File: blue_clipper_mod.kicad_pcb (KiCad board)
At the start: 2 copper layers, 68.6 x 50.8 mm, 23 parts, among them J1 AudioJack3, J2 AudioJack2, SW1 SW_Rotary_1x4_MP, SW2 SW_Rotary_1x4_MP, U1 RC4558

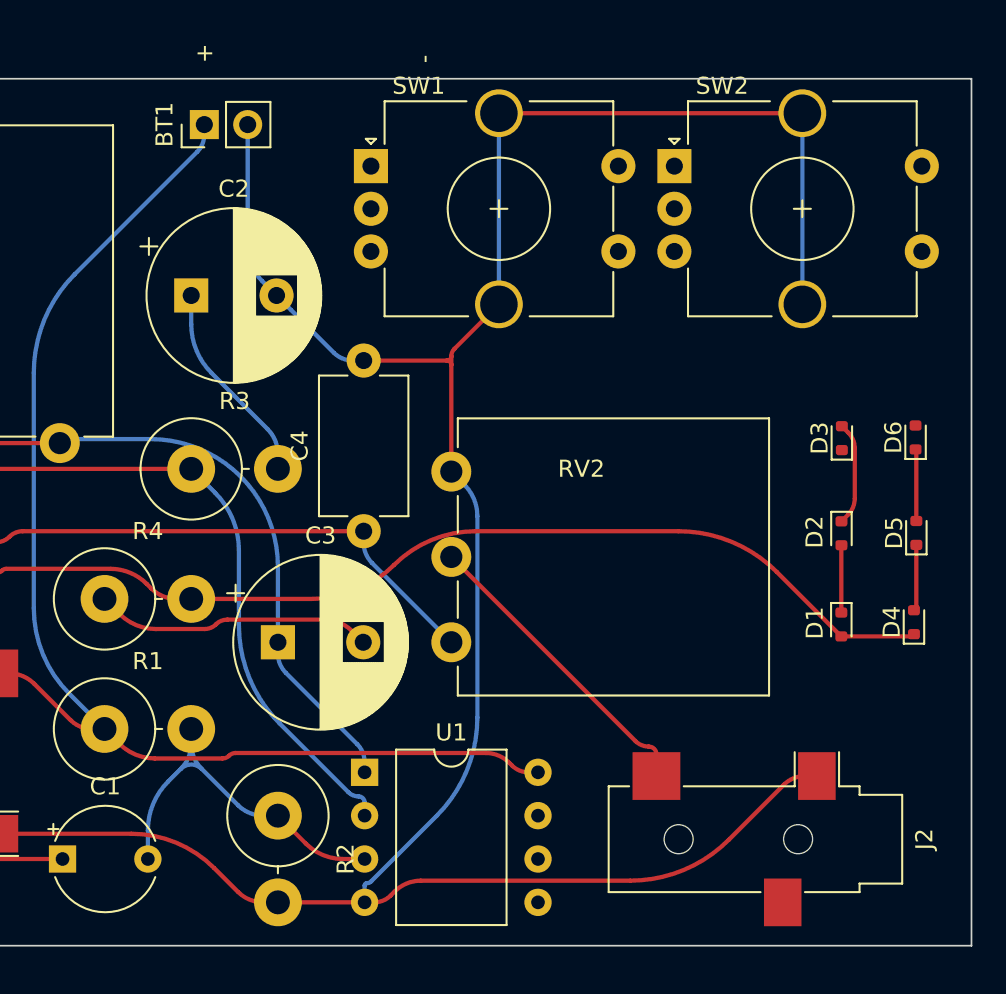
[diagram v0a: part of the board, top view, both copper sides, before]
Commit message: dangit one of the diodes was flipped the wrong way
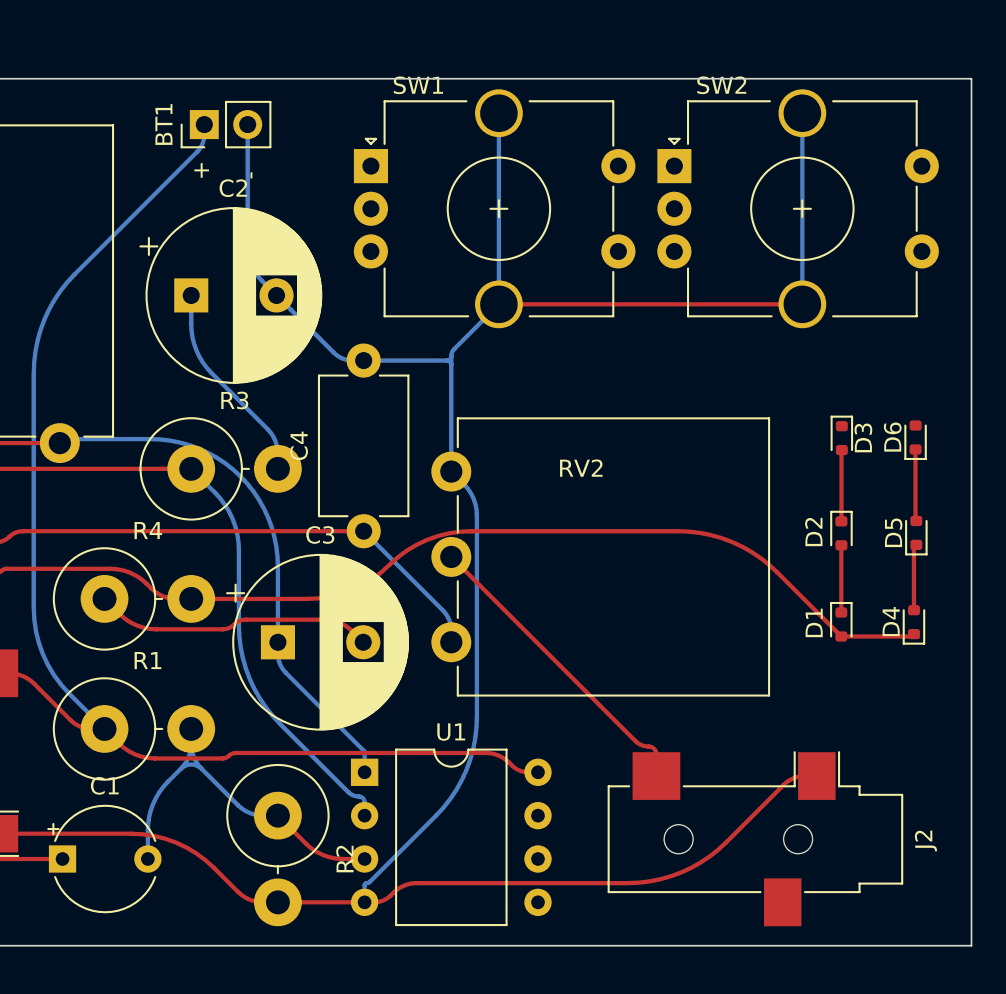
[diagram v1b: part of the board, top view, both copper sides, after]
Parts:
- turned D3 to -90 degrees
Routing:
- net Net-(D2-K): track 6.09 -> 4.18 mm

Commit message: reran autoroute
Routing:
- net Net-(U1A-+): track 22.8 -> 21.3 mm
- net /CLIPPER: track 64.5 -> 65.9 mm
- net GND: track 154.0 -> 155.3 mm
- net +9V: track 74.5 -> 75.8 mm
- net Net-(U1A--): track 42.3 -> 43.3 mm
- net Net-(C3-Pad1): track 36.1 -> 36.9 mm

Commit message: Revert "reran autoroute"
This reverts commit 381ba4100bb96fee684d495079d12acf929bcbfa.
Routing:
- net Net-(U1A-+): track 21.3 -> 22.8 mm
- net /CLIPPER: track 65.9 -> 64.5 mm
- net GND: track 155.3 -> 154.0 mm
- net +9V: track 75.8 -> 74.5 mm
- net Net-(U1A--): track 43.3 -> 42.3 mm
- net Net-(C3-Pad1): track 36.9 -> 36.1 mm

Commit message: fix everything
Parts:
- added H1: MountingHole, MountingHole:MountingHole_3.2mm_M3, F.Cu at (178.4, 50.2)
- added H2: MountingHole, MountingHole:MountingHole_3.2mm_M3, F.Cu at (137.2, 50.2)
- added H3: MountingHole, MountingHole:MountingHole_3.2mm_M3, F.Cu at (178.4, 64.1)
- added H4: MountingHole, MountingHole:MountingHole_3.2mm_M3, F.Cu at (137.2, 64.1)
- added JP1: SolderJumper_2_Open, Jumper:SolderJumper-2_P1.3mm_Open_RoundedPad1.0x1.5mm, F.Cu at (144.8, 47.8)
- added JP2: SolderJumper_2_Open, Jumper:SolderJumper-2_P1.3mm_Open_RoundedPad1.0x1.5mm, F.Cu at (157.5, 47.8)
- added R6: 50k, Resistor_SMD:R_0603_1608Metric_Pad0.98x0.95mm_HandSolder, F.Cu at (144.8, 50.0)
- added R7: 50k, Resistor_SMD:R_0603_1608Metric_Pad0.98x0.95mm_HandSolder, F.Cu at (157.5, 50.0)
- added SW3: BYPASS, Connector_PinHeader_2.54mm:PinHeader_1x06_P2.54mm_Vertical, F.Cu at (155.4, 64.8)
- C1: footprint Capacitor_THT:CP_Radial_Tantal_D6.0mm_P5.00mm -> Capacitor_SMD:C_0603_1608Metric
- C2, C3: footprint Capacitor_THT:CP_Radial_D10.0mm_P5.00mm -> Capacitor_THT:CP_Radial_D4.0mm_P1.50mm
- C4: footprint Capacitor_THT:C_Disc_D8.0mm_W5.0mm_P10.00mm -> Capacitor_SMD:C_0603_1608Metric_Pad1.08x0.95mm_HandSolder
- J1: value AudioJack3 -> IN; footprint Connector_Audio:Jack_3.5mm_CUI_SJ-3523-SMT_Horizontal -> custom:jack_pads
- J2: value AudioJack2 -> OUT; footprint Connector_Audio:Jack_3.5mm_CUI_SJ-3523-SMT_Horizontal -> custom:jack_pads
- R1, R3, R4, R5: footprint Resistor_THT:R_Axial_DIN0614_L14.3mm_D5.7mm_P5.08mm_Vertical -> Resistor_SMD:R_0603_1608Metric_Pad0.98x0.95mm_HandSolder
- R2: value 240k -> 20k; footprint Resistor_THT:R_Axial_DIN0614_L14.3mm_D5.7mm_P5.08mm_Vertical -> Resistor_SMD:R_0603_1608Metric_Pad0.98x0.95mm_HandSolder
- RV1: value 200k -> 100k; footprint Potentiometer_THT:Potentiometer_Piher_PC-16_Single_Vertical -> Connector_PinHeader_2.54mm:PinHeader_1x03_P2.54mm_Vertical
- RV2: footprint Potentiometer_THT:Potentiometer_Piher_PC-16_Single_Vertical -> Connector_PinHeader_2.54mm:PinHeader_1x03_P2.54mm_Vertical
- SW1, SW2: value SW_Rotary_1x4_MP -> ~; footprint Rotary_Encoder:RotaryEncoder_Alps_EC12E-Switch_Vertical_H20mm_CircularMountingHoles -> Connector_PinHeader_2.54mm:PinHeader_1x05_P2.54mm_Vertical
- U1: footprint Package_DIP:DIP-8_W10.16mm -> Package_DIP:DIP-8_W7.62mm_Socket
- moved R5 141.9 mm to (164.2, 59.7)
- moved R4 133.2 mm to (161.0, 56.9)
- moved J1 131.6 mm to (139.7, 57.9), turned to -90 degrees
- moved C3 129.5 mm to (159.5, 52.6), turned to -90 degrees
- moved RV1 129.3 mm to (153.7, 48.3), turned to -90 degrees
- moved C1 129.3 mm to (142.7, 62.0)
- moved U1 129.3 mm to (155.4, 52.8), turned to -90 degrees
- moved R1 127.4 mm to (145.3, 56.9), turned to -90 degrees
- moved R2 121.8 mm to (145.3, 60.9)
- moved RV2 119.1 mm to (164.8, 62.5), turned to -90 degrees
- moved SW1 118.6 mm to (178.3, 58.4), turned to -90 degrees
- moved C4 117.1 mm to (160.6, 59.7), turned to 180 degrees
- moved BT1 116.9 mm to (170.2, 62.5)
- moved R3 115.7 mm to (145.3, 52.8), turned to 90 degrees
- moved J2 112.1 mm to (162.3, 66.3)
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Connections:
- C1 pad 1: Net-(C1-Pad1) -> /EFFECT_IN
- C3 pad 1: Net-(C3-Pad1) -> Net-(JP2-B)
- J1 pad T: +9V -> /IN
- J2 pad T: Net-(J2-PadT) -> /OUT
- R3 pad 1: Net-(U1A--) -> Net-(JP1-A)
- RV1 pad 1: Net-(C3-Pad1) -> Net-(JP2-A)
- RV1 pad 2: Net-(C3-Pad1) -> Net-(JP2-A)
- RV1 pad 3: Net-(U1A--) -> Net-(JP1-B)
- RV2 pad 2: Net-(J2-PadT) -> /EFFECT_OUT
- U1 pad 1: Net-(C3-Pad1) -> Net-(JP2-B)
- U1 pad 2: Net-(U1A--) -> Net-(JP1-A)
- U1 pad 5: (no net) -> GND
- U1 pad 6: (no net) -> GND
- U1 pad 7: (no net) -> unconnected-(U1-Pad7)
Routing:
- net GND: track 154.0 -> 0.00 mm, vias 0 -> 16
- net /CLIPPER: track 64.5 -> 9.50 mm
- net +9V: track 74.5 -> 28.3 mm, vias 0 -> 1
- net Net-(U1A--): track 42.3 -> 0.00 mm
- net Net-(C3-Pad1): track 36.1 -> 0.00 mm
- net Net-(C4-Pad1): track 31.5 -> 6.78 mm
- net Net-(J2-PadT): track 18.1 -> 0.00 mm
- net Net-(JP1-A): track 0.00 -> 15.8 mm
- net /IN: track 0.00 -> 14.0 mm
- net Net-(C1-Pad1): track 13.4 -> 0.00 mm
- net Net-(C3-Pad2): track 16.3 -> 3.03 mm
- net /OUT: track 0.00 -> 11.6 mm
- net Net-(U1A-+): track 22.8 -> 12.0 mm
- net Net-(JP2-B): track 0.00 -> 9.52 mm
- net /EFFECT_OUT: track 0.00 -> 8.40 mm
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- added copper zone on B.Cu, net GND
- added copper zone on F.Cu, net GND
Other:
- board size 68.6 x 50.8 mm -> 48.9 x 21.6 mm
